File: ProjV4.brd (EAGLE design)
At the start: 100 x 80 mm, 30 parts, among them IC1 CD4007UBM, IC2 CD4007UBM, IC3 CD4007UBM, U1 MIC5504-3.3YM5-T5, U2 MCP2200-I/MQ, U3 ATMEGA328PB-AU, U4 EN11-HSM1BF20, Y1 CSTNE12M0G55A000R0

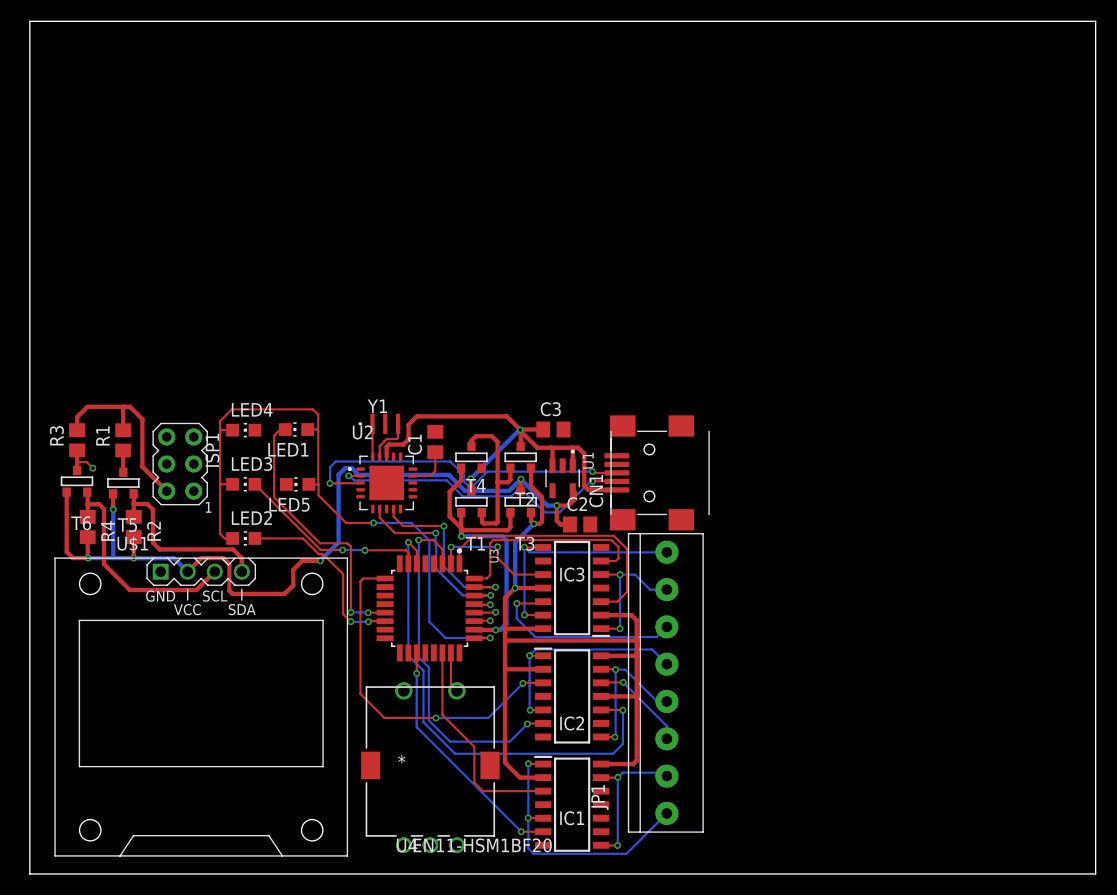
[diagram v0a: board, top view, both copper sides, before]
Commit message: Added copies of old versions
Updated version numbers and add old versions for comparison and report writing
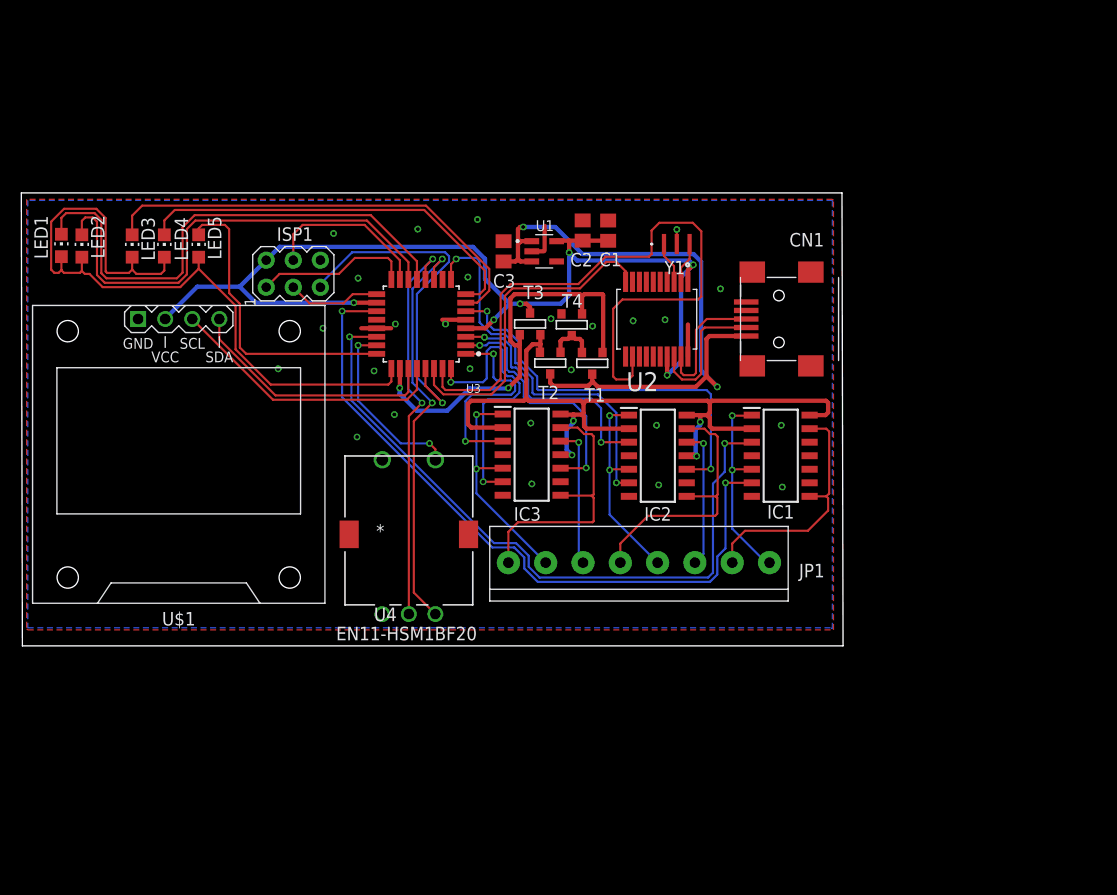
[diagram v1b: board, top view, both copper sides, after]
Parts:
- removed R1, R2, R3, R4: 10k, rcl:R0805
- removed T5, T6: (no value), zetex:SOT-23
- U2: value MCP2200-I/MQ -> MCP2200-I/SS; device MCP2200-I_MQ:QFN65P500X500X100-21N -> MCP2200-I_SS:SOP65P780X200-20N
- moved IC1 38.1 mm to (70.5, 39.2)
- moved Y1 32.1 mm to (60.7, 59.1)
- moved LED2 31.4 mm to (4.88, 58.9), turned to 0 degrees
- moved U2 29.6 mm to (58.8, 52.0), turned to 270 degrees
- moved LED1 28.0 mm to (2.96, 59.0), turned to 0 degrees
- moved C2 27.6 mm to (51.9, 60.4), turned to 90 degrees
- moved U3 26.7 mm to (36.7, 51.6), turned to 180 degrees
- moved C1 25.6 mm to (54.3, 60.4)
- moved LED3 24.7 mm to (9.60, 58.9), turned to 0 degrees
- moved LED5 24.2 mm to (15.8, 58.9), turned to 0 degrees
- moved IC2 24.0 mm to (58.9, 39.2)
- moved U$1 23.8 mm to (14.0, 39.4)
- moved U4 21.8 mm to (35.6, 16.5)
- moved U1 21.4 mm to (48.3, 58.4), turned to 0 degrees
- moved ISP1 20.8 mm to (24.7, 56.3), turned to 90 degrees
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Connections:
- removed net N$10: U2.7, U3.30
- removed net N$11: U2.9, U3.31
- removed net N$16: R2.1, T5.2, U$1.4
- removed net N$19: R4.1, T6.2, U$1.3
- removed net N$7: C1.1, U2.14
- new net RX/TX: U2.10, U3.30
- new net TX/RX: U2.12, U3.31
- net +3V3: now also C1.1, ISP1.2, U2.1, U2.17, U3.18, U3.4; no longer R2.2, R4.2, T5.3, T6.3
- net +5V: no longer ISP1.2, R1.2, R3.2, U2.18, U3.18, U3.4
- net 0: now also U2.20; no longer U2.1, U2.17, U2.21
- net C4: now also IC2.13, IC2.8; no longer IC2.1, IC2.5
- net C5: now also IC2.1, IC2.5; no longer IC2.13, IC2.8
- net D+: now also U2.19; no longer U2.3
- net D-: now also U2.18; no longer U2.2
- net LC4: now also IC2.6; no longer IC2.3
- net LC5: now also IC2.3; no longer IC2.6
- net N$14: now also U2.3; no longer U2.20
- net N$6: now also U2.2; no longer U2.19
- net SCL: now also U$1.3; no longer R3.1, T6.1
- net SDA: now also U$1.4; no longer R1.1, T5.1
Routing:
- net TX/RX: track 0.00 -> 64.0 mm
- net LC8: track 20.2 -> 65.4 mm, vias 0 -> 2
- net LC7: track 22.9 -> 66.0 mm
- net SW: track 0.00 -> 39.0 mm, vias 0 -> 2
- net LED4: track 0.00 -> 37.9 mm
- net CLK: track 0.00 -> 37.5 mm, vias 0 -> 2
- net RST: track 1.53 -> 34.1 mm
- net RX/TX: track 0.00 -> 31.1 mm
- net LED5: track 0.00 -> 28.4 mm
- net LED2: track 17.7 -> 45.7 mm, vias 2 -> 0
- net LED3: track 18.1 -> 42.9 mm, vias 2 -> 0
- net LED1: track 25.6 -> 49.0 mm, vias 2 -> 0
- net N$19: track 21.3 -> 0.00 mm
- net D+: track 33.4 -> 12.3 mm, vias 2 -> 0
- net SCL: track 5.62 -> 26.6 mm, vias 2 -> 0
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- added copper zone on layer 1, net 0
- added copper zone on layer 16, net 0
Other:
- board size 100 x 80 mm -> 77.1 x 42.5 mm
- board text added: "11/10/20 Version 2"
- board text added: "Marcel Vieira"
- board text added: "Pattern Generator"
- board text added: "https://github.com/mvieira4/ECE-388-Pattern-Gerator-Git"
